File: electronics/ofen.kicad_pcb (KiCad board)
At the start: 2 copper layers, 100.3 x 76.2 mm, 58 parts, among them J1 motor, J2 DC, J3 Screw_Terminal_01x03, J4 Screw_Terminal_01x03, Q1 Q_NPN_CBE, Q2 Q_NPN_CBE, Q3 Q_NPN_CBE, Q4 Q_NPN_CBE, Q5 BTA16-600B, SW1 SW_SPST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

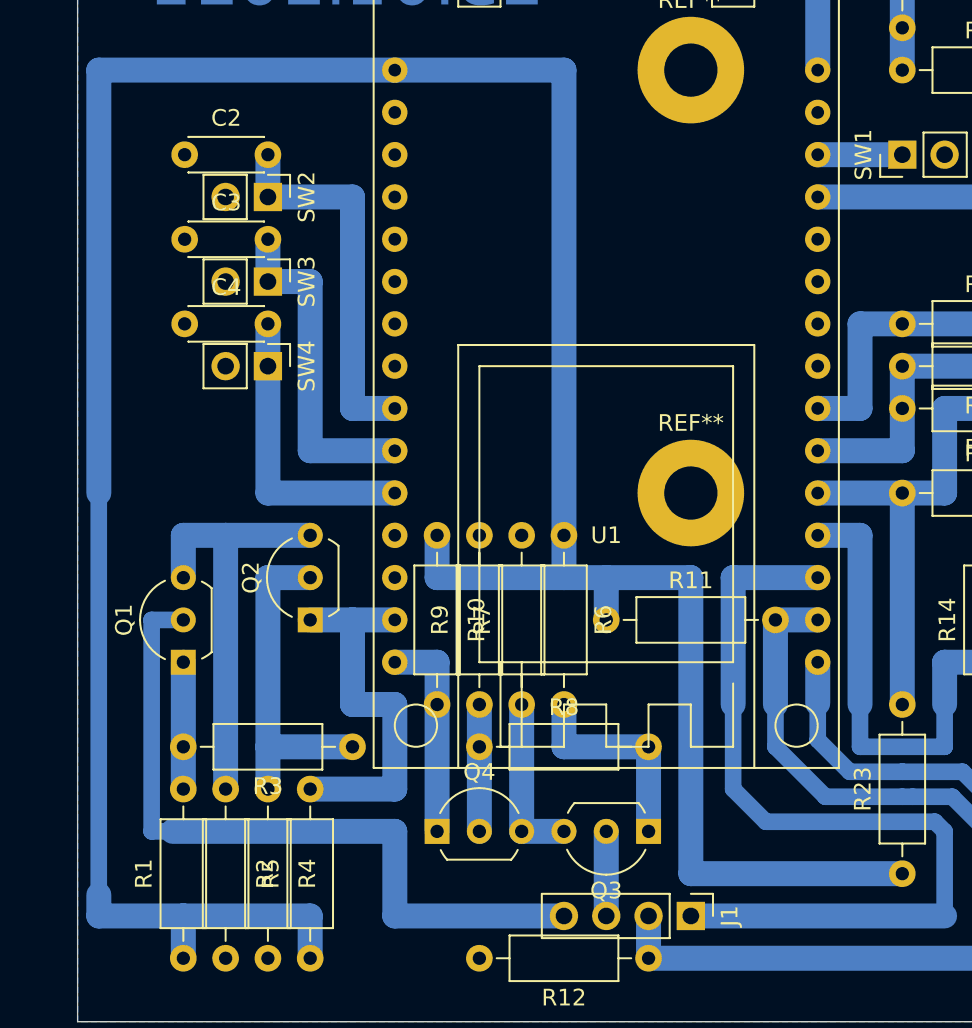
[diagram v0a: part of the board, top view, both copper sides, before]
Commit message: increased ground zone clearance to 0.8mm, updated KiCad version to 5.1.9
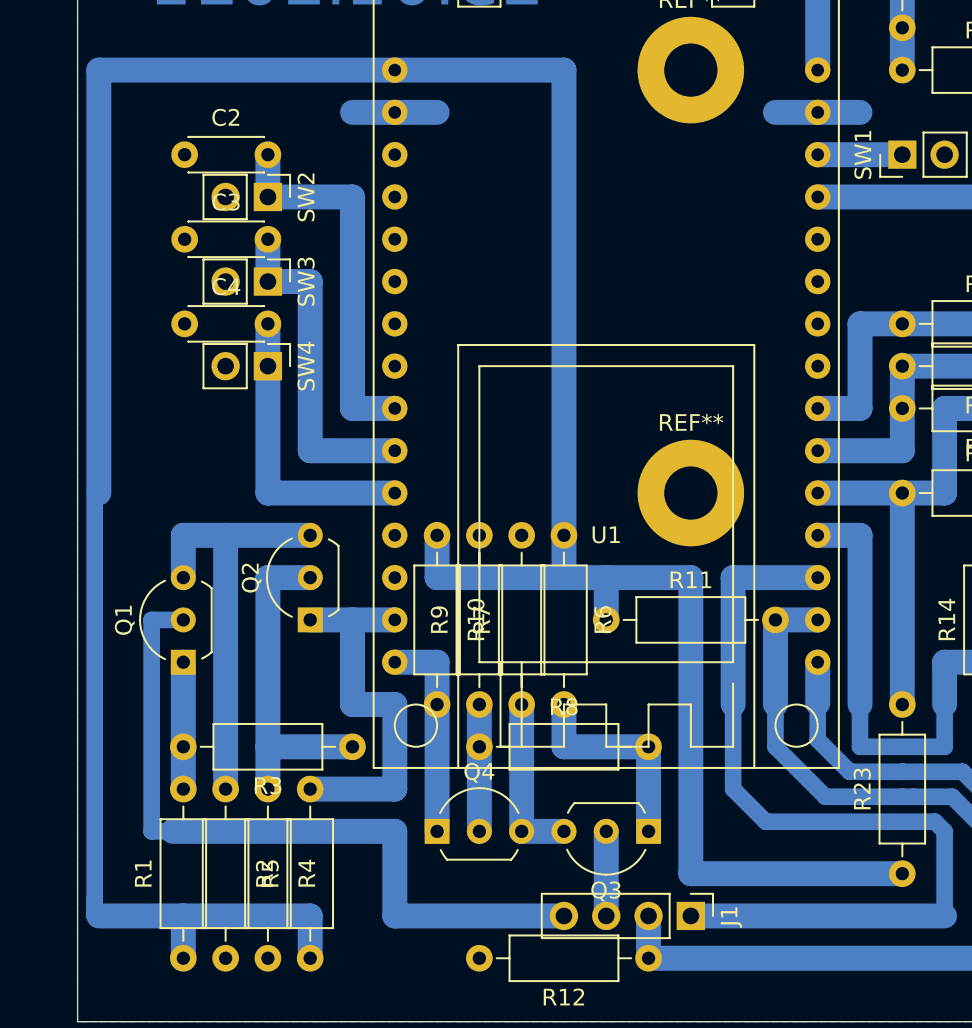
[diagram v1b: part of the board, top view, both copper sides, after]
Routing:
- net GND: track 0.00 -> 10.2 mm
- net +3V3: track 177.8 -> 178.8 mm
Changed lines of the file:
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@@
-(kicad_pcb (version 20171130) (host pcbnew 5.1.6+dfsg1-1)
+(kicad_pcb (version 20171130) (host pcbnew 5.1.9-73d0e3b20d~88~ubuntu20.10.1)
   (general
     (thickness 1.6)
     (drawings 5)
-    (tracks 187)
+    (tracks 189)
     (zones 0)
     (modules 58)
@@
     (user_trace_width 1.5)
     (trace_clearance 0.5)
-    (zone_clearance 0.5)
+    (zone_clearance 0.8)
     (zone_45_only no)
     (trace_min 0.2)
@@
       (effects (font (size 1 1) (thickness 0.15)))
     )
+    (fp_circle (center 0 0) (end 3.2 0) (layer Cmts.User) (width 0.15))
+    (fp_circle (center 0 0) (end 3.45 0) (layer F.CrtYd) (width 0.05))
     (fp_text user %R (at 0.3 0) (layer F.Fab)
       (effects (font (size 1 1) (thickness 0.15)))
     )
-    (fp_circle (center 0 0) (end 3.2 0) (layer Cmts.User) (width 0.15))
-    (fp_circle (center 0 0) (end 3.45 0) (layer F.CrtYd) (width 0.05))
     (pad 1 thru_hole circle (at 0 0) (size 6.4 6.4) (drill 3.2) (layers *.Cu *.Mask)
       (net 2 GND))
@@
       (effects (font (size 1 1) (thickness 0.15)))
     )
+    (fp_circle (center 0 0) (end 3.2 0) (layer Cmts.User) (width 0.15))
+    (fp_circle (center 0 0) (end 3.45 0) (layer F.CrtYd) (width 0.05))
     (fp_text user %R (at 0.3 0) (layer F.Fab)
       (effects (font (size 1 1) (thickness 0.15)))
     )
-    (fp_circle (center 0 0) (end 3.2 0) (layer Cmts.User) (width 0.15))
-    (fp_circle (center 0 0) (end 3.45 0) (layer F.CrtYd) (width 0.05))
     (pad 1 thru_hole circle (at 0 0) (size 6.4 6.4) (drill 3.2) (layers *.Cu *.Mask)
       (net 2 GND))
@@
       (effects (font (size 1 1) (thickness 0.15)))
     )
+    (fp_circle (center 0 0) (end 3.2 0) (layer Cmts.User) (width 0.15))
+    (fp_circle (center 0 0) (end 3.45 0) (layer F.CrtYd) (width 0.05))
     (fp_text user %R (at 0.3 0) (layer F.Fab)
       (effects (font (size 1 1) (thickness 0.15)))
     )
-    (fp_circle (center 0 0) (end 3.2 0) (layer Cmts.User) (width 0.15))
-    (fp_circle (center 0 0) (end 3.45 0) (layer F.CrtYd) (width 0.05))
     (pad 1 thru_hole circle (at 0 0) (size 6.4 6.4) (drill 3.2) (layers *.Cu *.Mask)
       (net 2 GND))
@@
       (effects (font (size 1 1) (thickness 0.15)))
     )
+    (fp_circle (center 0 0) (end 3.2 0) (layer Cmts.User) (width 0.15))
+    (fp_circle (center 0 0) (end 3.45 0) (layer F.CrtYd) (width 0.05))
     (fp_text user %R (at 0.3 0) (layer F.Fab)
       (effects (font (size 1 1) (thickness 0.15)))
     )
-    (fp_circle (center 0 0) (end 3.2 0) (layer Cmts.User) (width 0.15))
-    (fp_circle (center 0 0) (end 3.45 0) (layer F.CrtYd) (width 0.05))
     (pad 1 thru_hole circle (at 0 0) (size 6.4 6.4) (drill 3.2) (layers *.Cu *.Mask))
   )
@@
   (segment (start 162.56 114.234887) (end 162.56 116.421334) (width 1) (layer B.Cu) (net 1))
   (segment (start 162.56 116.421334) (end 164.478676 118.34001) (width 1) (layer B.Cu) (net 1))
+  (segment (start 139.7 78.74) (end 134.62 78.74) (width 1.5) (layer B.Cu) (net 2))
+  (segment (start 165.1 78.74) (end 160.02 78.74) (width 1.5) (layer B.Cu) (net 2))
   (segment (start 134.62 83.82) (end 129.54 83.82) (width 1.5) (layer B.Cu) (net 3) (status 20))
   (segment (start 134.62 96.52) (end 134.62 83.82) (width 1.5) (layer B.Cu) (net 3))
@@
   (segment (start 187.96 63.5) (end 182.88 63.5) (width 1.5) (layer B.Cu) (net 26) (status 30))
   (segment (start 182.88 63.5) (end 177.8 63.5) (width 1.5) (layer B.Cu) (net 26) (status 30))
-  (segment (start 119.38 125.73) (end 119.38 101.6) (width 1) (layer B.Cu) (net 27))
   (segment (start 137.16 76.2) (end 119.38501 76.2) (width 1.5) (layer B.Cu) (net 27) (status 10))
   (segment (start 119.38501 76.2) (end 119.38501 101.6) (width 1.5) (layer B.Cu) (net 27))
-  (segment (start 119.38501 127) (end 119.38501 125.73) (width 1.5) (layer B.Cu) (net 27))
   (segment (start 124.46 127) (end 119.38501 127) (width 1.5) (layer B.Cu) (net 27))
   (segment (start 132.08 127) (end 124.46 127) (width 1.5) (layer B.Cu) (net 27))
@@
   (segment (start 139.7 106.68) (end 147.32 106.68) (width 1.5) (layer B.Cu) (net 27))
   (segment (start 139.7 104.14) (end 139.7 106.68) (width 1.5) (layer B.Cu) (net 27) (status 10))
+  (segment (start 119.13501 127) (end 119.13501 125.984) (width 1) (layer B.Cu) (net 27))
+  (segment (start 119.13501 101.6) (end 119.13501 127) (width 1) (layer B.Cu) (net 27))
   (segment (start 182.88 83.82) (end 162.56 83.82) (width 1.5) (layer B.Cu) (net 28) (status 20))
   (segment (start 182.88 78.74) (end 182.88 83.82) (width 1.5) (layer B.Cu) (net 28) (status 10))
@@
   (segment (start 208.28 106.76) (end 203.28 106.76) (width 4) (layer B.Cu) (net 54) (status 10))
   (zone (net 2) (net_name GND) (layer B.Cu) (hatch edge 0.508)
-    (connect_pads (clearance 0.5))
+    (connect_pads (clearance 0.8))
     (min_thickness 0.7)
     (fill yes (arc_segments 32) (thermal_gap 0.5) (thermal_bridge_width 1))

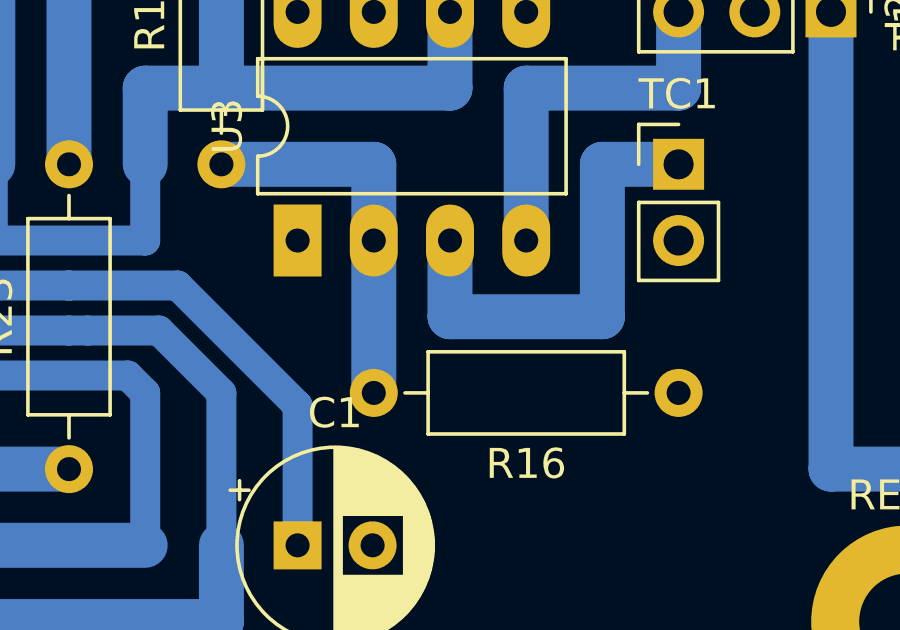
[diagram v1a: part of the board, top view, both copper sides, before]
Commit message: added resistor in parallel to the thermocouple to prevent OpAmp from destroying the ESP32
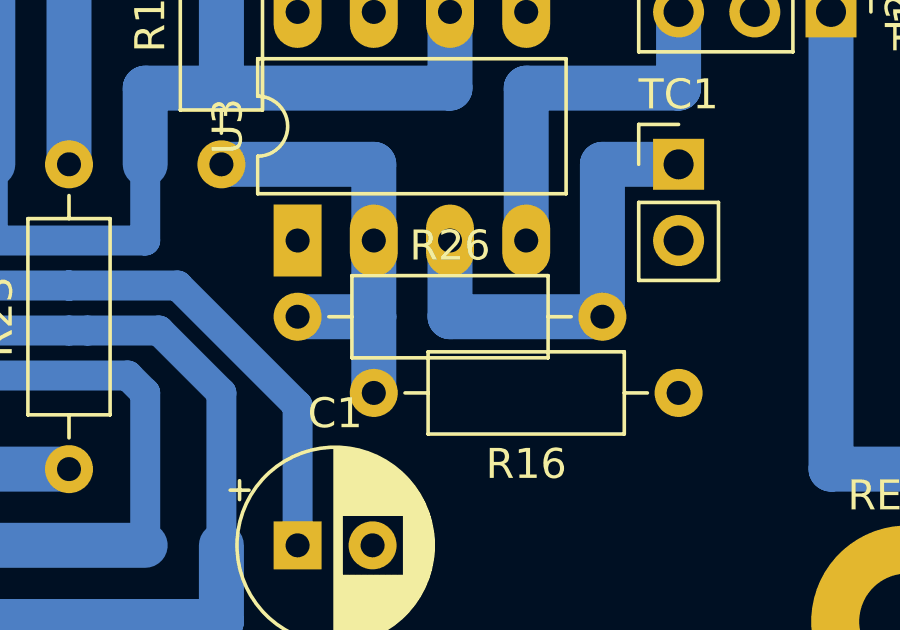
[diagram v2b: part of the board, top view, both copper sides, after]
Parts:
- added R26: 15k, Resistor_THT:R_Axial_DIN0207_L6.3mm_D2.5mm_P10.16mm_Horizontal, F.Cu at (175.3, 119.4)
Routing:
- net Net-(R14-Pad1): track 12.7 -> 15.2 mm

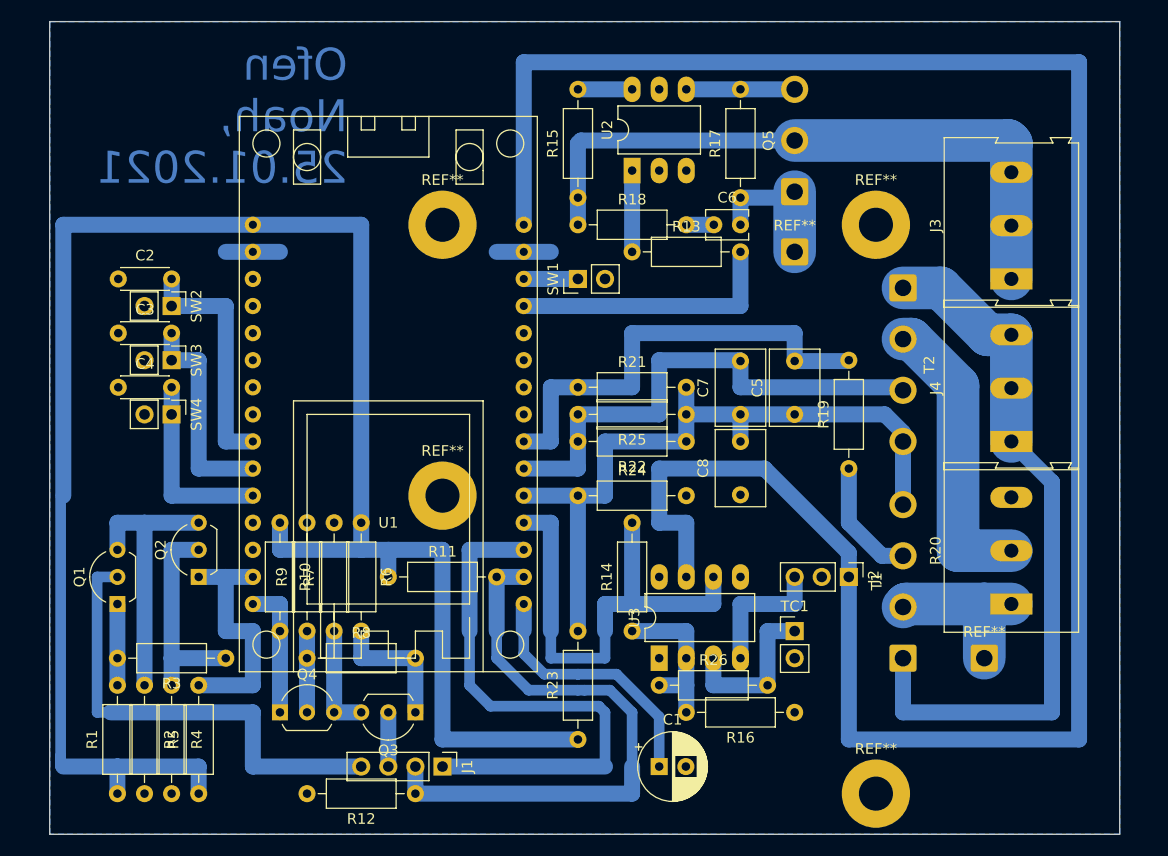
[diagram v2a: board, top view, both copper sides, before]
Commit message: arranged silkscreen and symbols properly
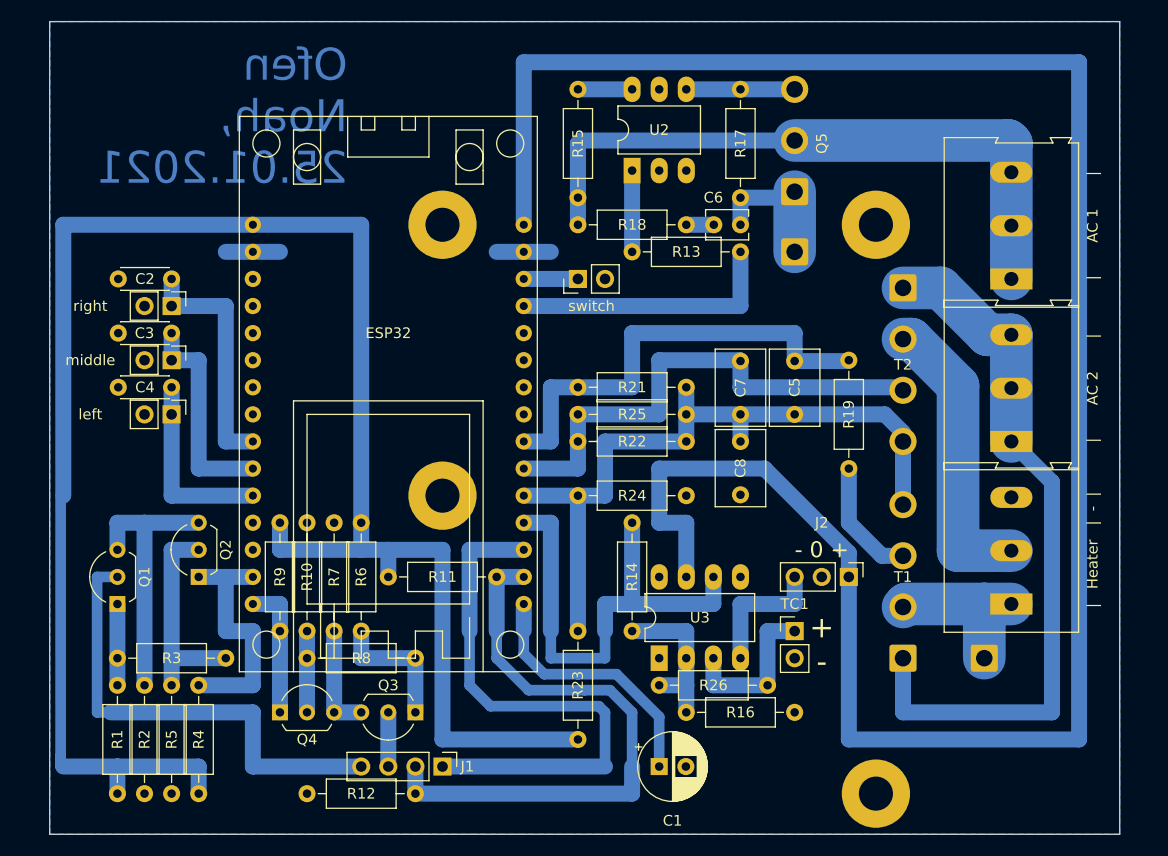
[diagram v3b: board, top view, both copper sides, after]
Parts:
- removed REF**: MountingHole_3.2mm_M3_Pad, MountingHole:MountingHole_3.2mm_M3_Pad
- added  : M3 mounting, MountingHole:MountingHole_3.2mm_M3_Pad, F.Cu at (195.6, 129.5)
-  : renamed from REF**; value MountingHole_3.2mm_M3_Pad -> M3 mounting (x3)
-  : renamed from REF**; value SolderWire-0.75sqmm_1x01_D1.25mm_OD2.3mm -> Wire bridge .75 (x2)
- Q1, Q2, Q3, Q4: value Q_NPN_CBE -> NPN
- T1: value Transformer_1P_1S -> Voltage Transformer
- T2: value Transformer_1P_1S -> Current transformer
- U3: value LMH6609MA -> OP27G
- left: renamed from SW4; value SW_Push -> left
- middle: renamed from SW3; value SW_Push -> middle
- right: renamed from SW2; value SW_Push -> right
- switch: renamed from SW1; value SW_SPST -> switch
- |       AC 1       |: renamed from J3; value Screw_Terminal_01x03 -> AC P
- |       AC 2       |: renamed from J4; value Screw_Terminal_01x03 -> AC N
- |   Heater   |  -  |: renamed from R20
- renumbered U1 to ESP32
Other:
- board text added: "+ -"
- board text added: "- 0 +"

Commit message: added opamp offset trimmer to schematic and pcb
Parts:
- removed |       AC 1       |: AC P, TerminalBlock:TerminalBlock_Altech_AK300-3_P5.00mm
- removed |       AC 2       |: AC N, TerminalBlock:TerminalBlock_Altech_AK300-3_P5.00mm
- added J3: AC_IN, TerminalBlock:TerminalBlock_Altech_AK300-3_P5.00mm, F.Cu at (208.3, 86.4)
- added J4: AC_OUT, Connector_Wire:SolderWire-0.75sqmm_1x02_P4.8mm_D1.25mm_OD2.3mm, F.Cu at (208.3, 70.8)
- added J5: AC_OUT, Connector_Wire:SolderWire-0.75sqmm_1x02_P4.8mm_D1.25mm_OD2.3mm, F.Cu at (208.3, 96.2)
- added RV1: 10k, Connector_PinHeader_2.54mm:PinHeader_1x03_P2.54mm_Vertical, F.Cu at (180.3, 119.4)
- Q1, Q2, Q3, Q4: value NPN -> Q_NPN_CBE
- R20: renamed from |   Heater   |  -  |
- SW1: renamed from switch; value switch -> SW_SPST
- SW2: renamed from right; value right -> SW_Push
- SW3: renamed from middle; value middle -> SW_Push
- SW4: renamed from left; value left -> SW_Push
- T1: value Voltage Transformer -> Transformer_1P_1S
- T2: value Current transformer -> Transformer_1P_1S
- U3: value OP27G -> LM6361; footprint Package_DIP:DIP-8_W7.62mm_LongPads -> Package_DIP:DIP-8_W7.62mm_Socket_LongPads
- moved TC1 16.1 mm to (182.9, 129.5), turned to 90 degrees
- moved U3 8.03 mm to (182.9, 114.3), turned to 180 degrees
- moved R26 5.68 mm to (180.3, 121.9)
- moved R24 5.68 mm to (172.7, 99.1)
- moved C8 5.08 mm to (188.0, 101.6)
- moved J2 3.59 mm to (190.5, 106.7)
- moved R16 3.59 mm to (190.5, 124.5)
- moved R14 2.54 mm to (172.7, 116.8)
- turned C1 to 270 degrees
- renumbered ESP32 to U1
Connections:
-   pad 1: (no net) -> GND
- U1 pad 23: Net-(U1-Pad23) -> GND
- U1 pad 24: Net-(U1-Pad24) -> GND
- U1 pad 25: Net-(U1-Pad25) -> GND
- U1 pad 26: Net-(U1-Pad26) -> GND
- U1 pad 3: Net-(U1-Pad3) -> GND
- U1 pad 4: Net-(U1-Pad4) -> GND
- U1 pad 5: Net-(U1-Pad5) -> GND
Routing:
- net +3V3: track 178.8 -> 158.9 mm
- net Net-(R14-Pad1): track 15.2 -> 32.0 mm
- net Net-(R26-Pad2): track 15.2 -> 28.9 mm
- net Net-(R14-Pad2): track 45.7 -> 33.2 mm
- net -5V: track 12.7 -> 2.54 mm
- net Net-(C5-Pad2): track 43.3 -> 36.0 mm
- net Net-(RV1-Pad1): track 0.00 -> 7.18 mm
- net Net-(RV1-Pad3): track 0.00 -> 6.13 mm
- net Net-(J3-Pad1): track 68.0 -> 62.1 mm
- net Net-(C7-Pad2): track 47.7 -> 42.4 mm
- net Net-(J3-Pad3): track 61.2 -> 56.8 mm
- net Net-(J1-Pad4): track 44.4 -> 40.8 mm
- net Net-(C3-Pad2): track 20.3 -> 16.9 mm
- net Net-(Q2-Pad1): track 22.9 -> 19.8 mm
- net Net-(C4-Pad2): track 17.8 -> 14.7 mm
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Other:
- board text added: "Ofen v2 Noah, 27.02.2021"
- board text removed: "+ -"
- board text removed: "Ofen Noah, 25.01.2021"
